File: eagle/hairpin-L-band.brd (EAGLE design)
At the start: 27 x 40 mm, 14 parts, among them J1 142-0701-851_TEST, J2 142-0701-851_TEST

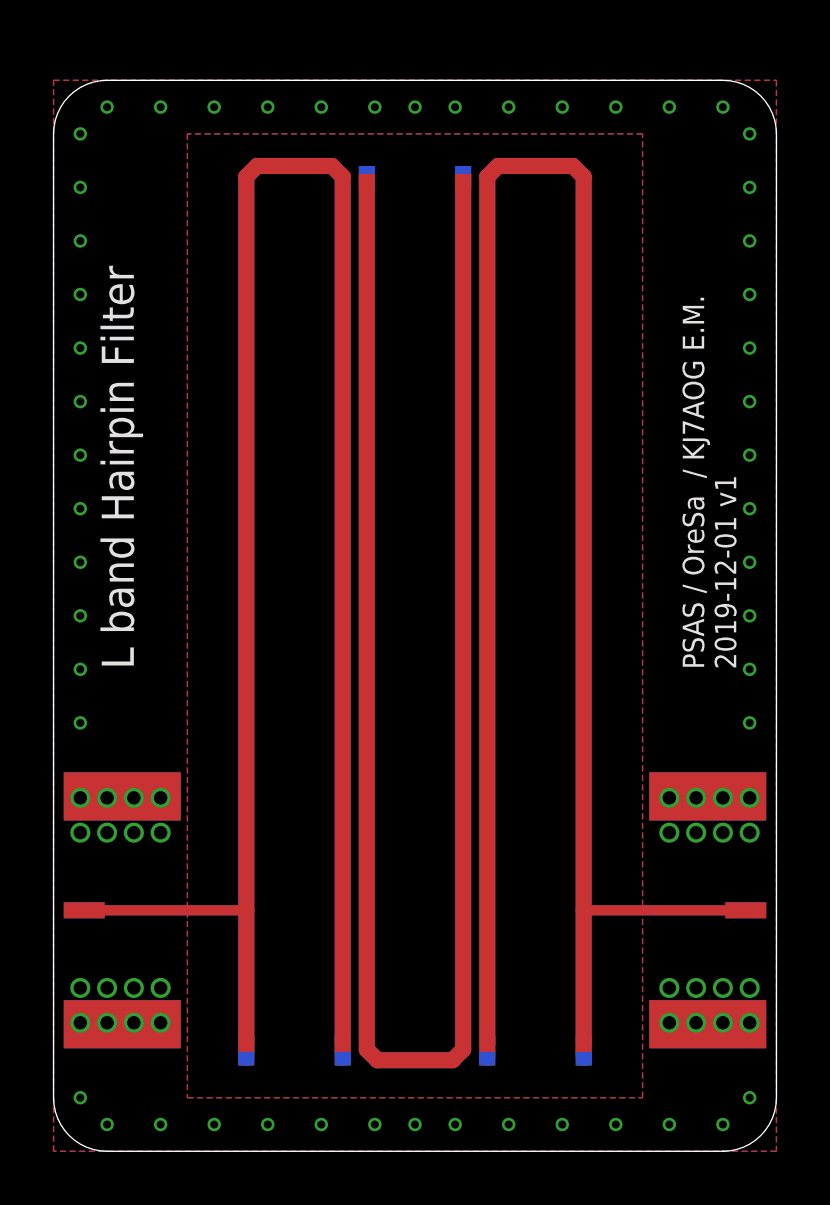
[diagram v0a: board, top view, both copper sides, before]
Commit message: Update L band hairpin
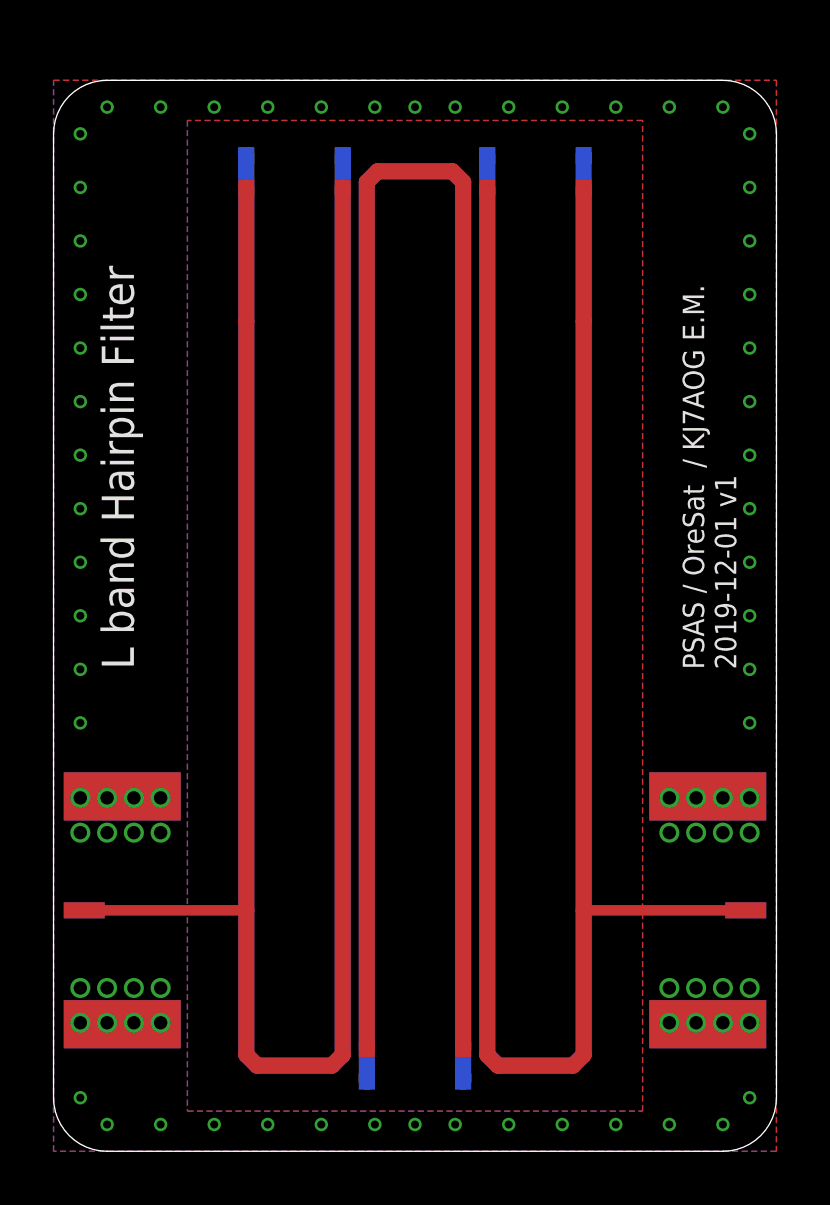
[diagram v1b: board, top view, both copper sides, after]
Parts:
- moved U$11 36.0 mm to (7.20, 37.2), turned to 180 degrees
- moved U$7 36.0 mm to (19.8, 37.2), turned to 180 degrees
- moved U$1 34.4 mm to (19.8, 36.0), turned to 180 degrees
- moved U$5 34.4 mm to (7.20, 36.0), turned to 180 degrees
- moved U$12 34.1 mm to (10.8, 37.2), turned to 180 degrees
- moved U$8 34.1 mm to (16.2, 37.2), turned to 180 degrees
- moved U$10 34.1 mm to (11.7, 2.60), turned to 180 degrees
- moved U$9 34.1 mm to (15.3, 2.60), turned to 180 degrees
- moved U$3 32.6 mm to (15.3, 3.80), turned to 180 degrees
- moved U$4 32.6 mm to (11.7, 3.80), turned to 180 degrees
- moved U$2 32.5 mm to (16.2, 36.0), turned to 180 degrees
- moved U$6 32.5 mm to (10.8, 36.0), turned to 180 degrees
- moved J1 27.0 mm to (27.0, 9.00), turned to 270 degrees
- moved J2 27.0 mm to (0.00, 9.00), turned to 90 degrees
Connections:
- net BLEFT: now also J2.RF2, U$11.END, U$12.END; no longer J1.RF2, U$7.END, U$8.END
- net BRIGHT: now also J1.RF2, U$7.END, U$8.END; no longer J2.RF2, U$11.END, U$12.END
- net TLEFT: now also J2.RF1, U$5.END, U$6.END; no longer J1.RF1, U$1.END, U$2.END
- net TRIGHT: now also J1.RF1, U$1.END, U$2.END; no longer J2.RF1, U$5.END, U$6.END
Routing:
- net BMID: track 69.3 -> 71.1 mm
- net BLEFT: track 75.8 -> 77.2 mm
- net BRIGHT: track 75.8 -> 77.2 mm
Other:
- board text removed: "PSAS / OreSa / KJ7AOG E.M. 2019-12-01 v1"

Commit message: Update L band hairpin
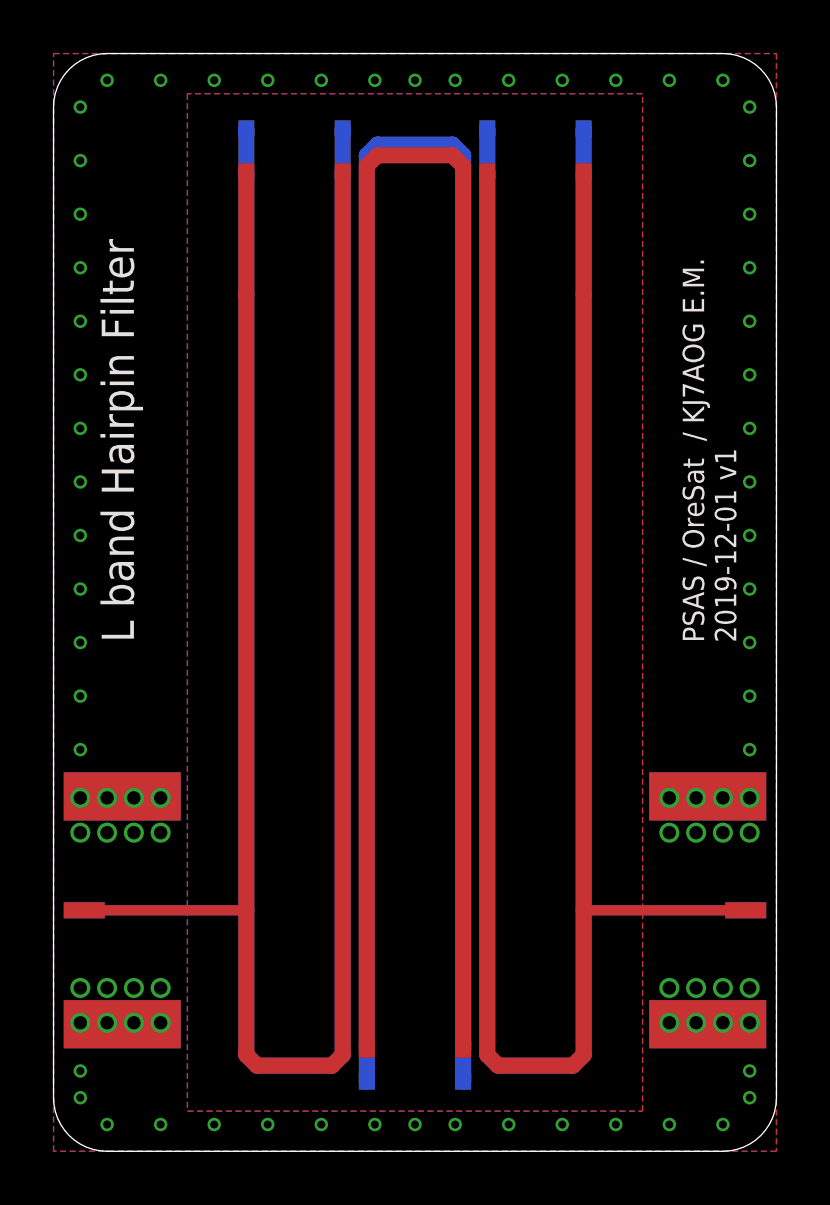
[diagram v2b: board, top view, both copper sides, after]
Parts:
- moved U$11 1.00 mm to (7.20, 38.2)
- moved U$12 1.00 mm to (10.8, 38.2)
- moved U$7 1.00 mm to (19.8, 38.2)
- moved U$8 1.00 mm to (16.2, 38.2)
- moved U$1 0.60 mm to (19.8, 36.6)
- moved U$2 0.60 mm to (16.2, 36.6)
- moved U$5 0.60 mm to (7.20, 36.6)
- moved U$6 0.60 mm to (10.8, 36.6)
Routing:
- net BRIGHT: track 77.2 -> 79.2 mm
- net BMID: track 71.1 -> 73.1 mm
- net BLEFT: track 77.2 -> 79.2 mm
- net TRIGHT: track 74.8 -> 76.0 mm
- net TMID: track 68.7 -> 69.9 mm
- net TLEFT: track 74.8 -> 76.0 mm
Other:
- board size 27 x 40 mm -> 27 x 41 mm
